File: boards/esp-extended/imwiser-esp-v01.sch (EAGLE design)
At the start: 15 parts, among them J1-A3 PJ-313-SPAD, J2-A2 PJ-313-SPAD, J3-A1 PJ-313-SPAD, J4-D3 PJ-313-SPAD, J5-D5 PJ-313-SPAD, J6-D6 PJ-313-SPAD, U1 ARDUINO_SHIELDNO_SILK

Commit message: Organized files, left organize cam jobs and libraries
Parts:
- removed CURRENT: (no value), SparkFun-Connectors:M02PTH
- removed J1-A3, J2-A2, J3-A1, J4-D3, J5-D5: PJ-313-SPAD, salvador-parts:PJ-313-SPAD
- added C2: 10uF, SparkFun-Capacitors:10UF-25V-20%(PTH)
- added C3, C4: 100nF, SparkFun-Capacitors:CAPPTH
- added C5: 47uF, SparkFun-Capacitors:10UF-25V-20%(PTH)
- added CURRENT0, CURRENT1, PROG: 2PIN, SparkFun-Connectors:M02PTH
- added D1, D2: 1N5817, adafruit:SCHOTTKY-DIODEDO41-7
- added ESP: ESP01, esp8266-modules:ESP01
- added ESP-CON: 3PIN, SparkFun-Connectors:M03PTH
- added J1-A2, J2-A3, J3-A4, J4-A5, J5-D9, J7-D5, J8-D3: PJ-313-SPAD, salvador-parts:PJ-313-SPAD
- added Q1, Q2: MOSFET-NCHANNEL2N7000, SparkFun-DiscreteSemi:MOSFET-NCHANNEL2N7000
- added R10, R11, R12, R9: 2.2K, resistor:R-US_0207/10
- added R13, R14, R15: 10K, resistor:R-US_0207/10
- added R5: 64, resistor:R-US_0207/10
- added R6: 82, resistor:R-US_0207/10
- added R7, R8: 470K, resistor:R-US_0207/10
- added REG: 78D33, salvador-parts-imported:V_REG_78XXSINK
- added S1: SWITCH-MOMENTARY-2PTH, salvador-parts-imported2:SWITCH-MOMENTARY-2PTH
- C1: value (none) -> 10uF
- D2-3, DOUT: value (none) -> 3PIN
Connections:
- net J5 renamed D6
- removed net N$10: CURRENT.2, R1.2, R2.2, U1.A0
- removed net N$11: C1.+, CURRENT.1, R1.1, R2.1, R3.1, R4.2
- removed net N$13: D2-3.1, J4-D3.SHIELD1, U1.*D3
- removed net N$3: J1-A3.SHIELD1, U1.A3
- removed net N$4: J2-A2.SHIELD1, U1.A2
- removed net N$5: J3-A1.SHIELD1, U1.A1
- removed net N$6: J5-D5.SHIELD1, U1.*D5
- new net 3.3V: C5.+, ESP.VCC, Q1.G, Q2.G, R11.2, R13.2, R14.2, R15.2, R9.2, REG.OUT
- new net A0: CURRENT0.2, R5.2, R6.2, U1.A0
- new net A1: CURRENT1.2, R1.2, R2.2, U1.A1
- new net A2: J1-A2.SHIELD1, U1.A2
- new net A3: J2-A3.SHIELD1, U1.A3
- new net A4: J3-A4.SHIELD1, U1.A4
- new net A5: J4-A5.SHIELD1, U1.A5
- new net BURDEN-C0: C2.+, CURRENT0.1, R5.1, R6.1, R7.1, R8.2
- new net BURDEN-C1: C1.+, CURRENT1.1, R1.1, R2.1, R3.1, R4.2
- new net CH-PD: C3.1, ESP.CH_PD, R14.1
- new net D3: D2-3.1, J8-D3.SHIELD1, U1.*D3
- new net D5: J7-D5.SHIELD2, U1.*D5
- new net D9: J5-D9.SHIELD2, U1.*D9
- new net DTR: D2.C, ESP-CON.3
- new net ESP-RX: ESP.RXD, Q2.S, R11.1
- new net ESP-TX: ESP.TXD, Q1.S, R9.1
- new net GPIO0: D1.A, ESP.GPIO0, PROG.1, R13.1
- new net N$16: J5-D9.L2, J6-D6.L1
- new net RST: ESP.RST, R15.1, S1.2
- new net U$1: C3.2, D1.C, D2.A
- new net UC-RX: ESP-CON.1, Q1.D, R10.1, U1.RX
- new net UC-TX: ESP-CON.2, Q2.D, R12.1, U1.TX
- net GND: now also C2.-, C4.2, C5.-, ESP.GND, J1-A2.R, J2-A3.R, J3-A4.R, J4-A5.R, J5-D9.R, J7-D5.R, J8-D3.R, PROG.2, R8.1, REG.GND, S1.1, S1.P$1; no longer J1-A3.R, J2-A2.R, J3-A1.R, J4-D3.R, J5-D5.R
- net N$1: now also J2-A3.L1, J3-A4.L2; no longer J1-A3.L2, J2-A2.L1
- net N$2: now also J1-A2.L1, J2-A3.L2; no longer J2-A2.L2, J3-A1.L1
- net N$7: now also J7-D5.L2, J8-D3.L1; no longer J4-D3.L1, J5-D5.L2
- net N$9: now also J7-D5.L1; no longer J5-D5.L1
- net VCC: now also C4.1, J3-A4.L1, J4-A5.L2, J8-D3.L2, R10.2, R12.2, R7.2, REG.IN; no longer J1-A3.L1, J4-D3.L2
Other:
- note added: "3.3V POWER SUPPLY"
- note added: "5V - 3.3V BIDIRECTIONAL UART CONVERTER"
- note added: "DIGITAL SENSORS/ACTUATORS"
- note added: "ESP8266"
- note added: "ESP8266 CONNECTOR"
- note added: "ESP8266 FTDI-AUTORESET"
- note added: "IMWiserNode - ARDUINO SHIELD Version 0.1"
- note removed: "DIGITAL SENSORS"
- moved on the sheet: C1, D2-3, DOUT, J6-D6, R1, R2, R3, R4, U1

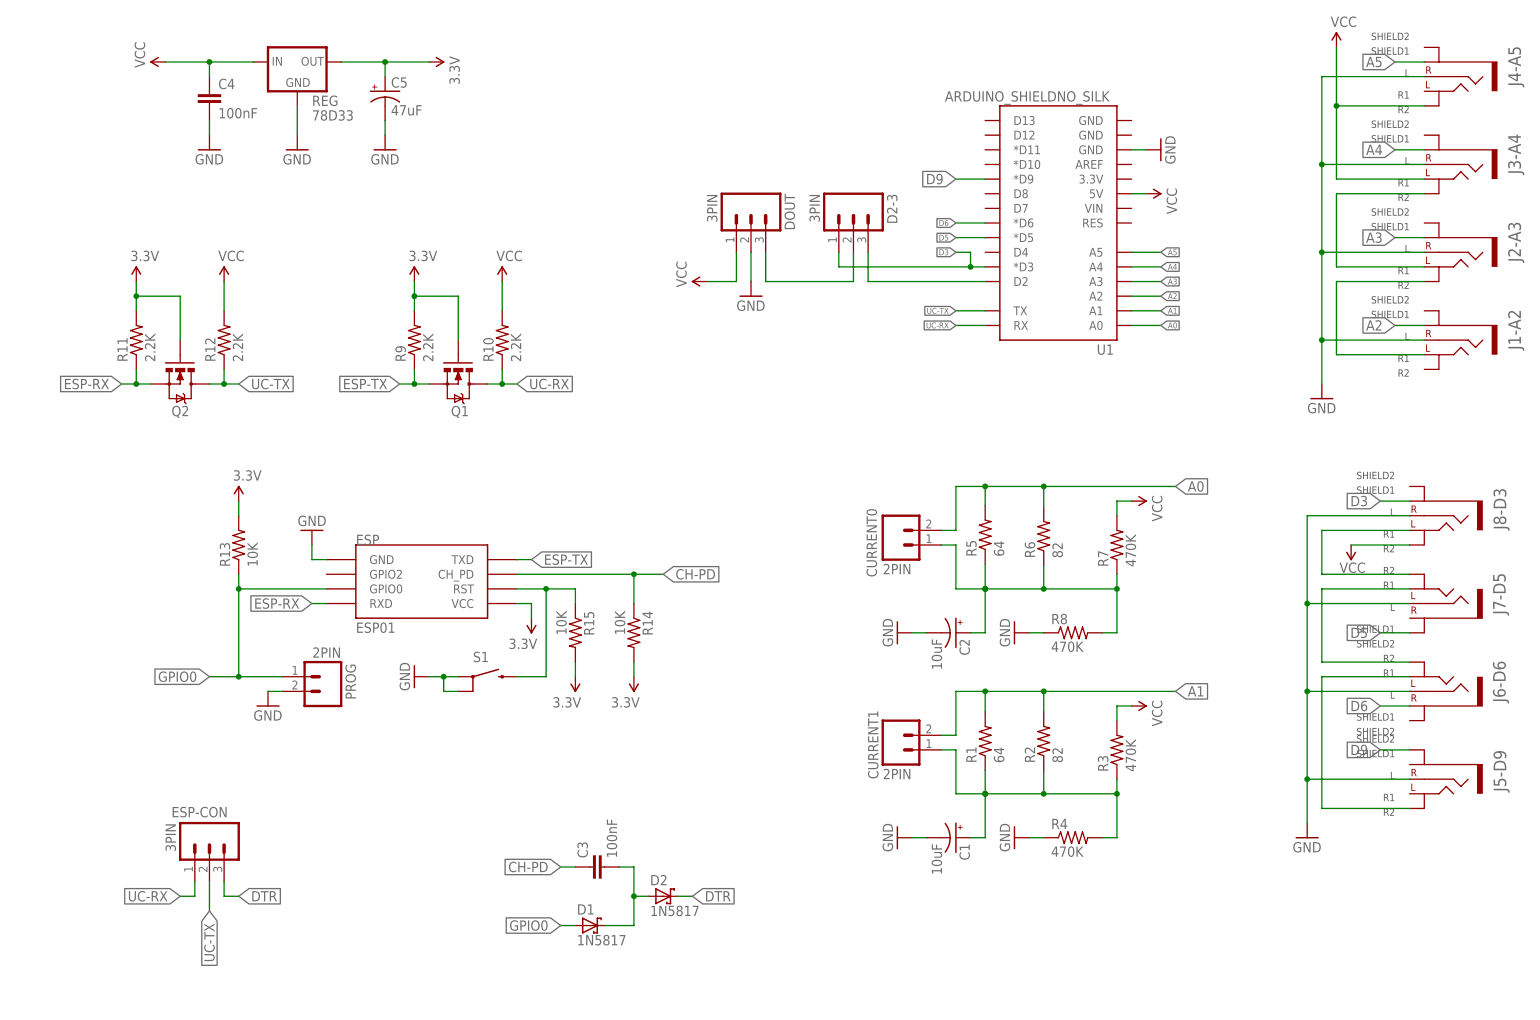
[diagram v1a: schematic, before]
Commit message: Finished version 0.1 of imwiser for ESP
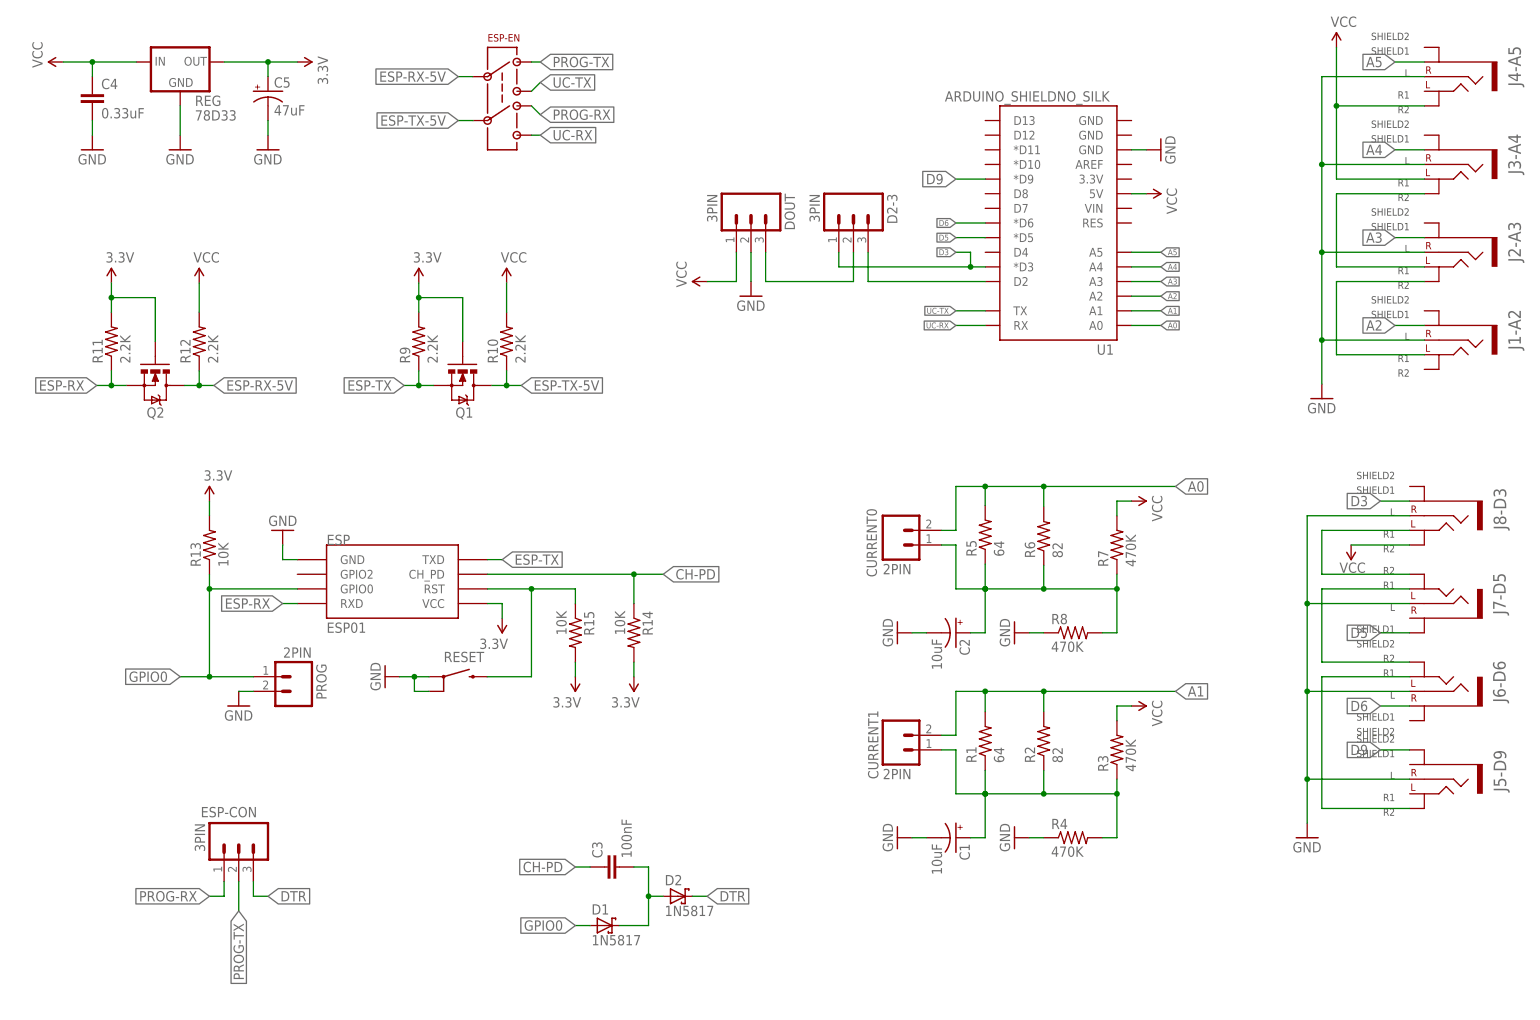
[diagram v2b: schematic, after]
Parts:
- removed S1: SWITCH-MOMENTARY-2PTH, salvador-parts-imported2:SWITCH-MOMENTARY-2PTH
- added ESP-EN: DPDT-GENERIC-SWITCH-7X7MM, salvador-parts:DPDT-GENERIC-SWITCH-7X7MM
- added RESET: SWITCH-MOMENTARY-2PTH, salvador-parts-imported2:SWITCH-MOMENTARY-2PTH
- C4: value 100nF -> 0.33uF
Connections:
- new net ESP-RX-5V: ESP-EN.IN1, Q2.D, R12.1
- new net ESP-TX-5V: ESP-EN.IN2, Q1.D, R10.1
- new net PROG-RX: ESP-CON.1, ESP-EN.OUT2-A
- new net PROG-TX: ESP-CON.2, ESP-EN.OUT1-A
- net GND: now also RESET.1, RESET.P$1; no longer S1.1, S1.P$1
- net RST: now also RESET.2; no longer S1.2
- net UC-RX: now also ESP-EN.OUT2-B; no longer ESP-CON.1, Q1.D, R10.1
- net UC-TX: now also ESP-EN.OUT1-B; no longer ESP-CON.2, Q2.D, R12.1
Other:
- note added: "ESP-CON SELECTOR"
- moved on the sheet: C3, C4, C5, D1, D2, ESP, ESP-CON, PROG, Q1, Q2, R10, R11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
